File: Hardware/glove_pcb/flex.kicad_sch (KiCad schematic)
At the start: 9 parts

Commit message: More work on motor driver connection
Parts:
- removed RV2, RV3, RV4, RV5, RV6, RV7, RV8, RV9: R_Potentiometer, symbol Device:R_Potentiometer
- RV1: value R_Potentiometer -> 10k
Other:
- moved on the sheet: RV1
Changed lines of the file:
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@@
 (kicad_sch (version 20230121) (generator eeschema)
   (paper "A4")
-  (symbol (lib_id "Device:R_Potentiometer") (at 124.46 45.72 0) (unit 1)
+  (symbol (lib_id "Device:R_Potentiometer") (at 50.8 41.91 0) (unit 1)
     (in_bom yes) (on_board yes) (dnp no) (fields_autoplaced)
-    (property "Reference" "RV4" (at 121.92 44.45 0)
+    (property "Reference" "RV1" (at 48.26 40.64 0)
       (effects (font (size 1.27 1.27)) (justify right))
     )
-    (property "Value" "R_Potentiometer" (at 121.92 46.99 0)
+    (property "Value" "10k" (at 48.26 43.18 0)
       (effects (font (size 1.27 1.27)) (justify right))
     )
-    (property "Footprint" "" (at 124.46 45.72 0)
+    (property "Footprint" "" (at 50.8 41.91 0)
       (effects (font (size 1.27 1.27)) hide)
     )
-    (property "Datasheet" "~" (at 124.46 45.72 0)
-      (effects (font (size 1.27 1.27)) hide)
-    )
-    (pin "1")
-    (pin "2")
-    (pin "3")
-    (instances
-      (project "glove_pcb"
-        (path "/747ff5f3-d342-40b0-8e4e-75b3a3063e75"
-          (reference "RV4") (unit 1)
-        )
-        (path "/747ff5f3-d342-40b0-8e4e-75b3a3063e75/bbbc9975-a050-48bd-8c18-11f2eff17087"
-          (reference "RV4") (unit 1)
-        )
-      )
-    )
-  )
-  (symbol (lib_id "Device:R_Potentiometer") (at 100.33 45.72 0) (unit 1)
-    (in_bom yes) (on_board yes) (dnp no) (fields_autoplaced)
-    (property "Reference" "RV3" (at 97.79 44.45 0)
-      (effects (font (size 1.27 1.27)) (justify right))
-    )
-    (property "Value" "R_Potentiometer" (at 97.79 46.99 0)
-      (effects (font (size 1.27 1.27)) (justify right))
-    )
-    (property "Footprint" "" (at 100.33 45.72 0)
-      (effects (font (size 1.27 1.27)) hide)
-    )
-    (property "Datasheet" "~" (at 100.33 45.72 0)
-      (effects (font (size 1.27 1.27)) hide)
-    )
-    (pin "1")
-    (pin "2")
-    (pin "3")
-    (instances
-      (project "glove_pcb"
-        (path "/747ff5f3-d342-40b0-8e4e-75b3a3063e75"
-          (reference "RV3") (unit 1)
-        )
-        (path "/747ff5f3-d342-40b0-8e4e-75b3a3063e75/bbbc9975-a050-48bd-8c18-11f2eff17087"
-          (reference "RV3") (unit 1)
-        )
-      )
-    )
-  )
-  (symbol (lib_id "Device:R_Potentiometer") (at 223.52 45.72 0) (unit 1)
-    (in_bom yes) (on_board yes) (dnp no) (fields_autoplaced)
-    (property "Reference" "RV8" (at 220.98 44.45 0)
-      (effects (font (size 1.27 1.27)) (justify right))
-    )
-    (property "Value" "R_Potentiometer" (at 220.98 46.99 0)
-      (effects (font (size 1.27 1.27)) (justify right))
-    )
-    (property "Footprint" "" (at 223.52 45.72 0)
-      (effects (font (size 1.27 1.27)) hide)
-    )
-    (property "Datasheet" "~" (at 223.52 45.72 0)
-      (effects (font (size 1.27 1.27)) hide)
-    )
-    (pin "1")
-    (pin "2")
-    (pin "3")
-    (instances
-      (project "glove_pcb"
-        (path "/747ff5f3-d342-40b0-8e4e-75b3a3063e75"
-          (reference "RV8") (unit 1)
-        )
-        (path "/747ff5f3-d342-40b0-8e4e-75b3a3063e75/bbbc9975-a050-48bd-8c18-11f2eff17087"
-          (reference "RV8") (unit 1)
-        )
-      )
-    )
-  )
-  (symbol (lib_id "Device:R_Potentiometer") (at 151.13 45.72 0) (unit 1)
-    (in_bom yes) (on_board yes) (dnp no) (fields_autoplaced)
-    (property "Reference" "RV5" (at 148.59 44.45 0)
-      (effects (font (size 1.27 1.27)) (justify right))
-    )
-    (property "Value" "R_Potentiometer" (at 148.59 46.99 0)
-      (effects (font (size 1.27 1.27)) (justify right))
-    )
-    (property "Footprint" "" (at 151.13 45.72 0)
-      (effects (font (size 1.27 1.27)) hide)
-    )
-    (property "Datasheet" "~" (at 151.13 45.72 0)
-      (effects (font (size 1.27 1.27)) hide)
-    )
-    (pin "1")
-    (pin "2")
-    (pin "3")
-    (instances
-      (project "glove_pcb"
-        (path "/747ff5f3-d342-40b0-8e4e-75b3a3063e75"
-          (reference "RV5") (unit 1)
-        )
-        (path "/747ff5f3-d342-40b0-8e4e-75b3a3063e75/bbbc9975-a050-48bd-8c18-11f2eff17087"
-          (reference "RV5") (unit 1)
-        )
-      )
-    )
-  )
-  (symbol (lib_id "Device:R_Potentiometer") (at 175.26 45.72 0) (unit 1)
-    (in_bom yes) (on_board yes) (dnp no) (fields_autoplaced)
-    (property "Reference" "RV6" (at 172.72 44.45 0)
-      (effects (font (size 1.27 1.27)) (justify right))
-    )
-    (property "Value" "R_Potentiometer" (at 172.72 46.99 0)
-      (effects (font (size 1.27 1.27)) (justify right))
-    )
-    (property "Footprint" "" (at 175.26 45.72 0)
-      (effects (font (size 1.27 1.27)) hide)
-    )
-    (property "Datasheet" "~" (at 175.26 45.72 0)
-      (effects (font (size 1.27 1.27)) hide)
-    )
-    (pin "1")
-    (pin "2")
-    (pin "3")
-    (instances
-      (project "glove_pcb"
-        (path "/747ff5f3-d342-40b0-8e4e-75b3a3063e75"
-          (reference "RV6") (unit 1)
-        )
-        (path "/747ff5f3-d342-40b0-8e4e-75b3a3063e75/bbbc9975-a050-48bd-8c18-11f2eff17087"
-          (reference "RV6") (unit 1)
-        )
-      )
-    )
-  )
-  (symbol (lib_id "Device:R_Potentiometer") (at 50.8 45.72 0) (unit 1)
-    (in_bom yes) (on_board yes) (dnp no) (fields_autoplaced)
-    (property "Reference" "RV1" (at 48.26 44.45 0)
-      (effects (font (size 1.27 1.27)) (justify right))
-    )
-    (property "Value" "R_Potentiometer" (at 48.26 46.99 0)
-      (effects (font (size 1.27 1.27)) (justify right))
-    )
-    (property "Footprint" "" (at 50.8 45.72 0)
-      (effects (font (size 1.27 1.27)) hide)
-    )
-    (property "Datasheet" "~" (at 50.8 45.72 0)
+    (property "Datasheet" "~" (at 50.8 41.91 0)
       (effects (font (size 1.27 1.27)) hide)
     )
@@
         )
       )
-    )
-  )
-  (symbol (lib_id "Device:R_Potentiometer") (at 74.93 45.72 0) (unit 1)
-    (in_bom yes) (on_board yes) (dnp no) (fields_autoplaced)
-    (property "Reference" "RV2" (at 72.39 44.45 0)
-      (effects (font (size 1.27 1.27)) (justify right))
-    )
-    (property "Value" "R_Potentiometer" (at 72.39 46.99 0)
-      (effects (font (size 1.27 1.27)) (justify right))
-    )
-    (property "Footprint" "" (at 74.93 45.72 0)
-      (effects (font (size 1.27 1.27)) hide)
-    )
-    (property "Datasheet" "~" (at 74.93 45.72 0)
-      (effects (font (size 1.27 1.27)) hide)
-    )
-    (pin "1")
-    (pin "2")
-    (pin "3")
-    (instances
-      (project "glove_pcb"
-        (path "/747ff5f3-d342-40b0-8e4e-75b3a3063e75"
-          (reference "RV2") (unit 1)
-        )
-        (path "/747ff5f3-d342-40b0-8e4e-75b3a3063e75/bbbc9975-a050-48bd-8c18-11f2eff17087"
-          (reference "RV2") (unit 1)
-        )
-      )
-    )
-  )
-  (symbol (lib_id "Device:R_Potentiometer") (at 199.39 45.72 0) (unit 1)
-    (in_bom yes) (on_board yes) (dnp no) (fields_autoplaced)
-    (property "Reference" "RV7" (at 196.85 44.45 0)
-      (effects (font (size 1.27 1.27)) (justify right))
-    )
-    (property "Value" "R_Potentiometer" (at 196.85 46.99 0)
-      (effects (font (size 1.27 1.27)) (justify right))
-    )
-    (property "Footprint" "" (at 199.39 45.72 0)
-      (effects (font (size 1.27 1.27)) hide)
-    )
-    (property "Datasheet" "~" (at 199.39 45.72 0)
-      (effects (font (size 1.27 1.27)) hide)
-    )
-    (pin "1")
-    (pin "2")
-    (pin "3")
-    (instances
-      (project "glove_pcb"
-        (path "/747ff5f3-d342-40b0-8e4e-75b3a3063e75"
-          (reference "RV7") (unit 1)
-        )
-        (path "/747ff5f3-d342-40b0-8e4e-75b3a3063e75/bbbc9975-a050-48bd-8c18-11f2eff17087"
-          (reference "RV7") (unit 1)
-        )
-      )
-    )
-  )
-  (symbol (lib_id "Device:R_Potentiometer") (at 247.65 45.72 0) (unit 1)
-    (in_bom yes) (on_board yes) (dnp no) (fields_autoplaced)
-    (property "Reference" "RV9" (at 245.11 44.45 0)
-      (effects (font (size 1.27 1.27)) (justify right))
-    )
-    (property "Value" "R_Potentiometer" (at 245.11 46.99 0)
-      (effects (font (size 1.27 1.27)) (justify right))
-    )
-    (property "Footprint" "" (at 247.65 45.72 0)
-      (effects (font (size 1.27 1.27)) hide)
-    )
-    (property "Datasheet" "~" (at 247.65 45.72 0)
-      (effects (font (size 1.27 1.27)) hide)
-    )
-    (pin "1")
-    (pin "2")
-    (pin "3")
-    (instances
-      (project "glove_pcb"
-        (path "/747ff5f3-d342-40b0-8e4e-75b3a3063e75"
-          (reference "RV9") (unit 1)
-        )
-        (path "/747ff5f3-d342-40b0-8e4e-75b3a3063e75/bbbc9975-a050-48bd-8c18-11f2eff17087"
-          (reference "RV9") (unit 1)
-        )
-      )

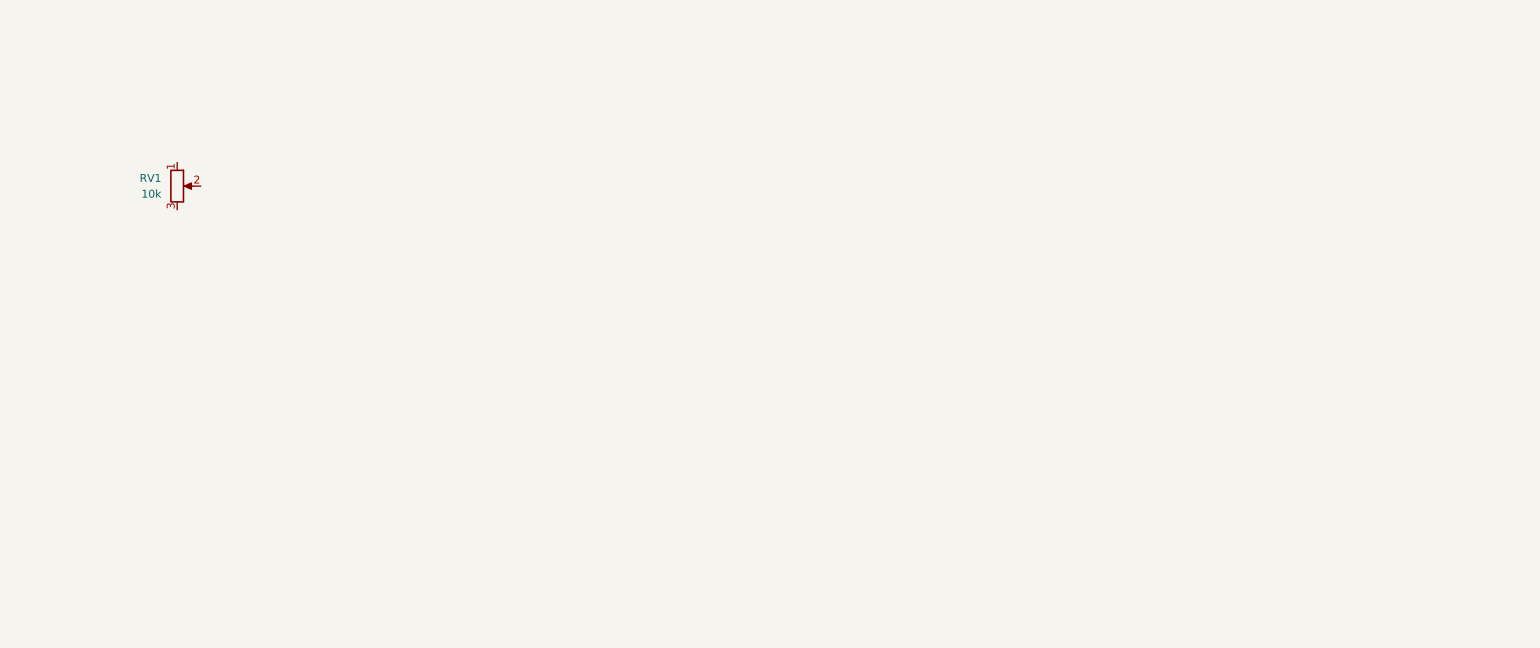
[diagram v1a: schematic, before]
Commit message: Replace offboard components with connectors, add uC, add example mux, fix motor wiring
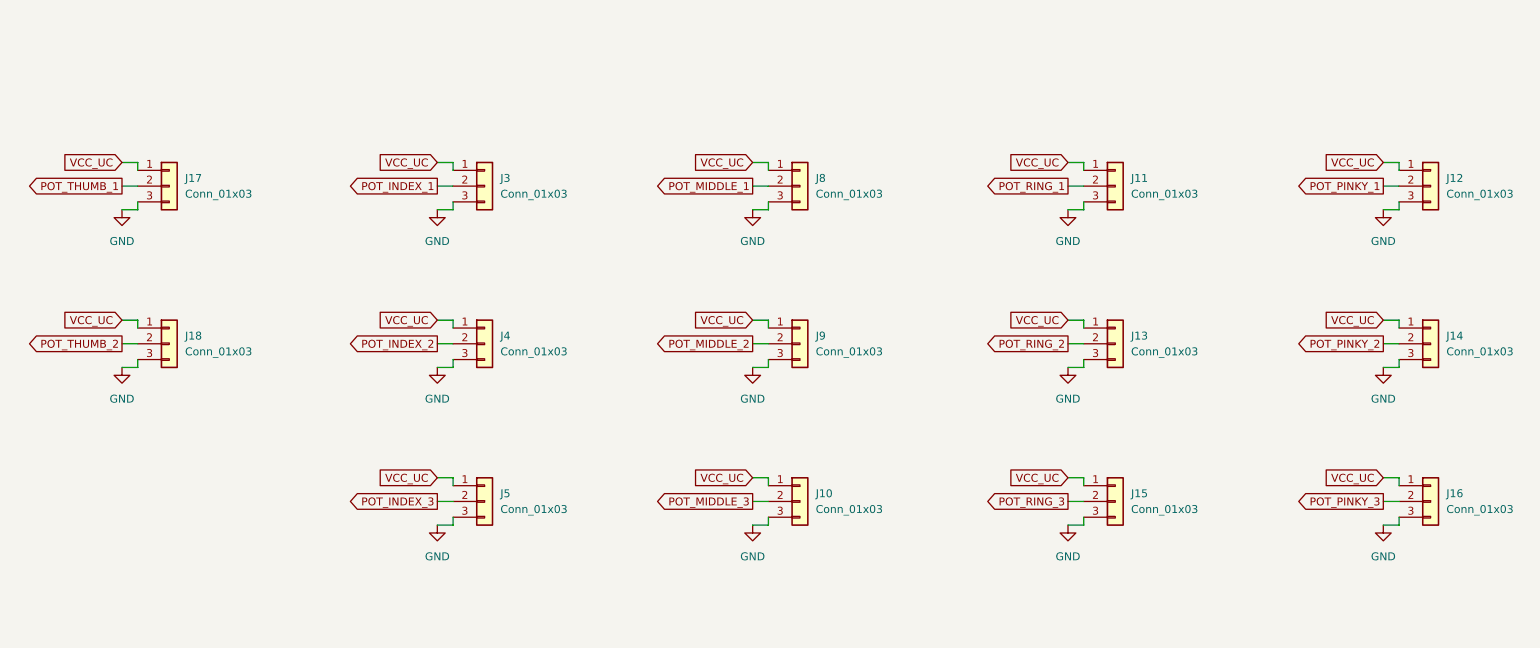
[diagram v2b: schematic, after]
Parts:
- removed RV1: 10k, symbol Device:R_Potentiometer
- added J10, J11, J12, J13, J14, J15, J16, J17, J18, J3, J4, J5, J8, J9: Conn_01x03, symbol Connector_Generic:Conn_01x03
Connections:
- new net GND: J10.3 (Pin_3), J11.3 (Pin_3), J12.3 (Pin_3), J13.3 (Pin_3), J14.3 (Pin_3), J15.3 (Pin_3), J16.3 (Pin_3), J17.3 (Pin_3), J18.3 (Pin_3), J3.3 (Pin_3), J4.3 (Pin_3), J5.3 (Pin_3), J8.3 (Pin_3), J9.3 (Pin_3)
- new net POT_INDEX_1: J3.2 (Pin_2)
- new net POT_INDEX_2: J4.2 (Pin_2)
- new net POT_INDEX_3: J5.2 (Pin_2)
- new net POT_MIDDLE_1: J8.2 (Pin_2)
- new net POT_MIDDLE_2: J9.2 (Pin_2)
- new net POT_MIDDLE_3: J10.2 (Pin_2)
- new net POT_PINKY_1: J12.2 (Pin_2)
- new net POT_PINKY_2: J14.2 (Pin_2)
- new net POT_PINKY_3: J16.2 (Pin_2)
- new net POT_RING_1: J11.2 (Pin_2)
- new net POT_RING_2: J13.2 (Pin_2)
- new net POT_RING_3: J15.2 (Pin_2)
- new net POT_THUMB_1: J17.2 (Pin_2)
- new net POT_THUMB_2: J18.2 (Pin_2)
- new net VCC_UC: J10.1 (Pin_1), J11.1 (Pin_1), J12.1 (Pin_1), J13.1 (Pin_1), J14.1 (Pin_1), J15.1 (Pin_1), J16.1 (Pin_1), J17.1 (Pin_1), J18.1 (Pin_1), J3.1 (Pin_1), J4.1 (Pin_1), J5.1 (Pin_1), J8.1 (Pin_1), J9.1 (Pin_1)

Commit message: Yet more improvements to the schematic
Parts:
- removed J10, J11, J12, J13, J14, J15, J16, J17, J18, J3, J4, J5, J8, J9: Conn_01x03, symbol Connector_Generic:Conn_01x03
- added J19: Potentiometers, symbol Connector_Generic:Conn_02x14_Odd_Even
- added R10, R11, R12, R13, R14, R15, R16, R17, R18, R19, R20, R7, R8, R9: 1k, symbol Device:R
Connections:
- net GND: now also J19.1 (Pin_1), J19.11 (Pin_11), J19.13 (Pin_13), J19.15 (Pin_15), J19.17 (Pin_17), J19.19 (Pin_19), J19.21 (Pin_21), J19.23 (Pin_23), J19.25 (Pin_25), J19.27 (Pin_27), J19.3 (Pin_3), J19.5 (Pin_5), J19.7 (Pin_7), J19.9 (Pin_9)
- net POT_INDEX_1: now also J19.6 (Pin_6), R9.2
- net POT_INDEX_2: now also J19.8 (Pin_8), R10.2
- net POT_INDEX_3: now also J19.10 (Pin_10), R11.2
- net POT_MIDDLE_1: now also J19.12 (Pin_12), R12.2
- net POT_MIDDLE_2: now also J19.14 (Pin_14), R13.2
- net POT_MIDDLE_3: now also J19.16 (Pin_16), R14.2
- net POT_PINKY_1: now also J19.24 (Pin_24), R16.1
- net POT_PINKY_2: now also J19.26 (Pin_26), R15.1
- net POT_PINKY_3: now also J19.28 (Pin_28), R18.2
- net POT_RING_1: now also J19.18 (Pin_18), R20.1
- net POT_RING_2: now also J19.20 (Pin_20), R19.1
- net POT_RING_3: now also J19.22 (Pin_22), R17.1
- net POT_THUMB_1: now also J19.2 (Pin_2), R7.2
- net POT_THUMB_2: now also J19.4 (Pin_4), R8.2
- net VCC_UC: now also R10.1, R11.1, R12.1, R13.1, R14.1, R15.2, R16.2, R17.2, R18.1, R19.2, R20.2, R7.1, R8.1, R9.1
